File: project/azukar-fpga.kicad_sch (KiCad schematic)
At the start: 11 parts

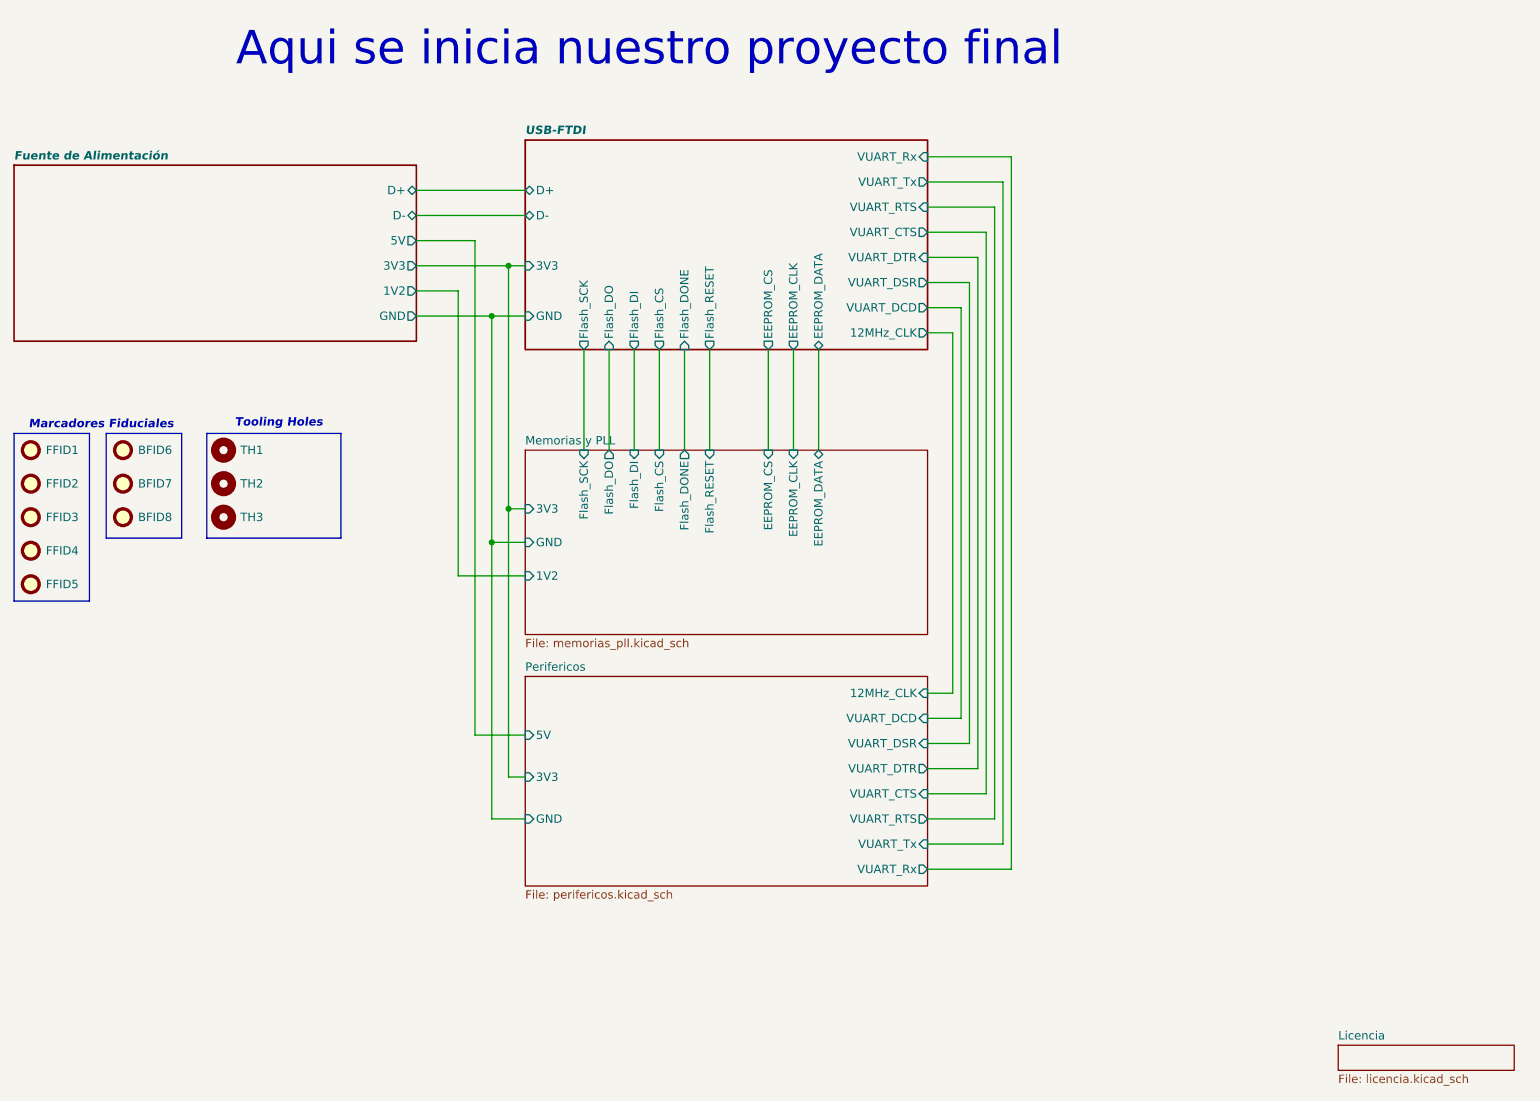
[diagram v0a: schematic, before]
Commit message: cambio a nombre final, agregado de licencia en esquematico y etiqueta
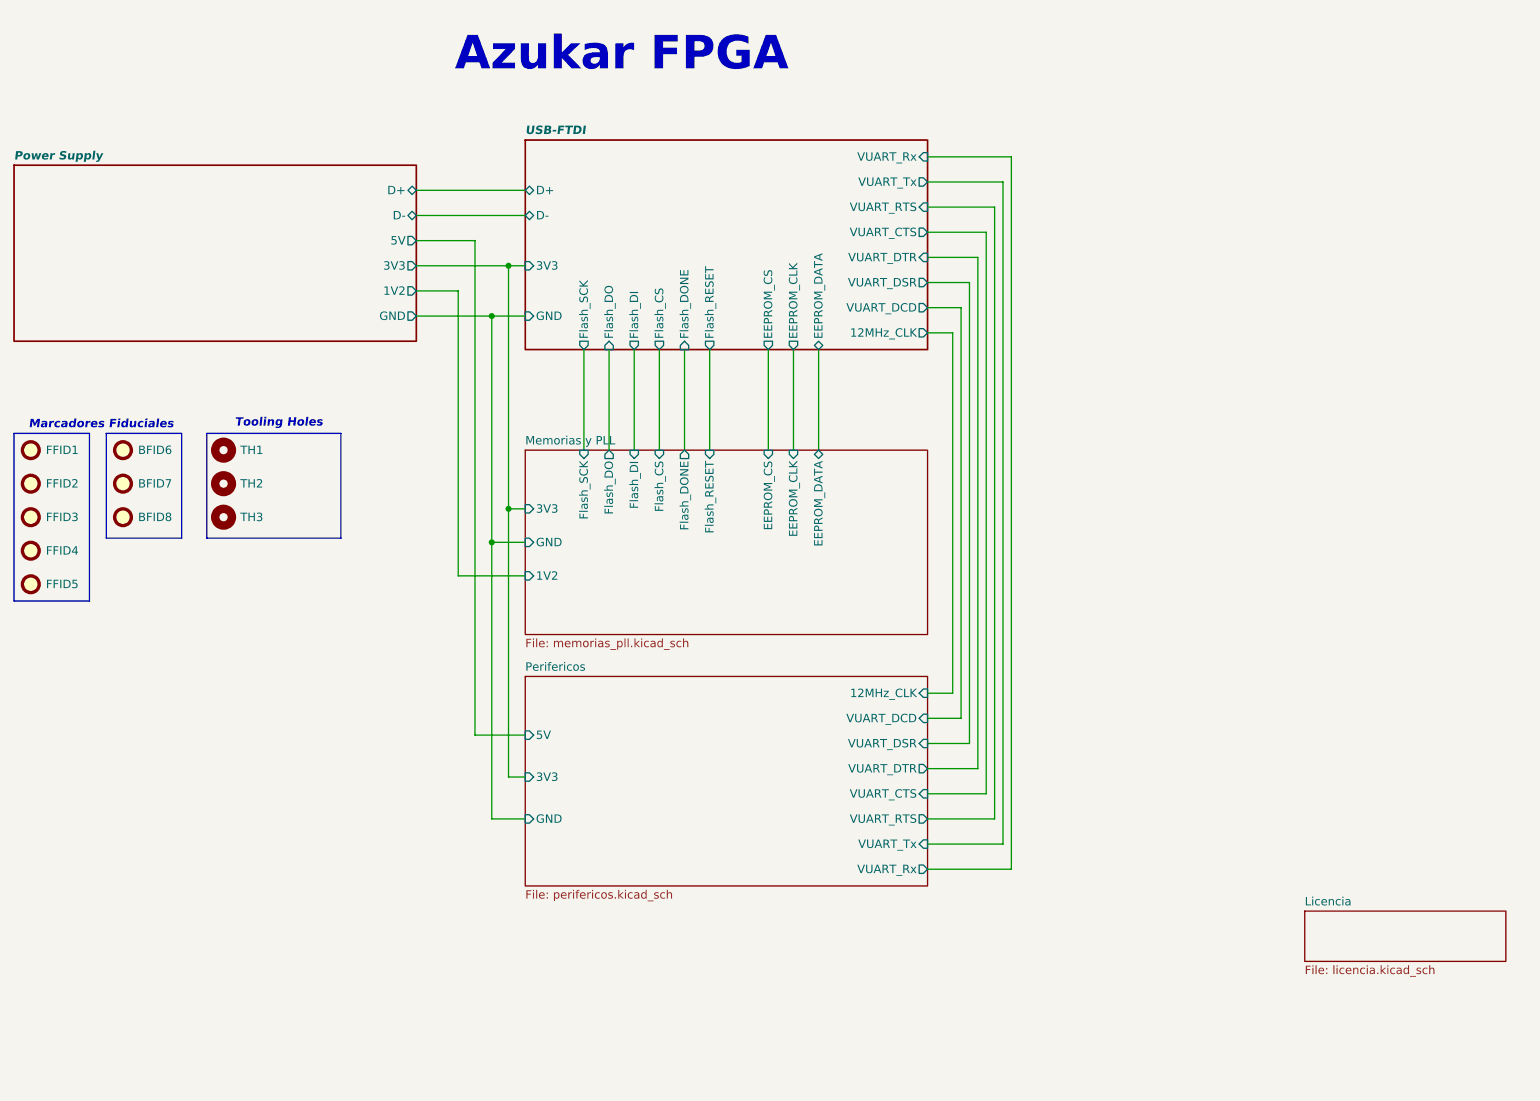
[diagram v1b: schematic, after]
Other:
- sheet Fuente de Alimentación renamed Power Supply
- note added: "Azukar FPGA"
- note removed: "Aqui se inicia nuestro proyecto final"
- company: (none) -> Maximiliano Simonazzi, Valentin Gomez Espeche
- title: (none) -> Azukar FPGA
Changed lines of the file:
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@@
 	(generator_version "9.0")
 	(paper "A4")
+	(title_block
+		(title "Azukar FPGA")
+		(date "2026-02-04")
+		(rev "1.4")
+		(company "Maximiliano Simonazzi, Valentin Gomez Espeche")
+		(comment 1 "attribution to the original AZUKAR project is preserved.")
+		(comment 2 "This design may be copied, modified, manufactured, and distributed provided that")
+		(comment 3 "Year: 2026")
+		(comment 4 "License: CERN Open Hardware Licence v2 – Permissive (CERN-OHL-P-2.0)")
+	)
 	(rectangle
 		(start 83.82 81.28)
@@
 		)
 	)
-	(text "Aqui se inicia nuestro proyecto final"
+	(text "Azukar FPGA"
 		(exclude_from_sim no)
-		(at 150.876 23.114 0)
+		(at 121.412 23.876 0)
 		(effects
 			(font
 				(size 5.08 5.08)
-			)
+				(thickness 1.016)
+				(bold yes)
+			)
+			(justify left)
 		)
 	)
@@
 		)
 		(instances
-			(project "fpga-utn"
+			(project "azukar-fpga"
 				(path "/fadb8841-cd7a-4174-937d-7c393e857c90"
 					(reference "FFID4")
@@
 		)
 		(instances
-			(project "fpga-utn"
+			(project "azukar-fpga"
 				(path "/fadb8841-cd7a-4174-937d-7c393e857c90"
 					(reference "FFID5")
@@
 		)
 		(instances
-			(project "fpga-utn"
+			(project "azukar-fpga"
 				(path "/fadb8841-cd7a-4174-937d-7c393e857c90"
 					(reference "BFID8")
@@
 		)
 		(instances
-			(project "fpga-utn"
+			(project "azukar-fpga"
 				(path "/fadb8841-cd7a-4174-937d-7c393e857c90"
 					(reference "FFID3")
@@
 		)
 		(instances
-			(project "fpga-utn"
+			(project "azukar-fpga"
 				(path "/fadb8841-cd7a-4174-937d-7c393e857c90"
 					(reference "BFID7")
@@
 		)
 		(instances
-			(project "fpga-utn"
+			(project "azukar-fpga"
 				(path "/fadb8841-cd7a-4174-937d-7c393e857c90"
 					(reference "FFID2")
@@
 		)
 		(instances
-			(project "fpga-utn"
+			(project "azukar-fpga"
 				(path "/fadb8841-cd7a-4174-937d-7c393e857c90"
 					(reference "BFID6")
@@
 		)
 		(instances
-			(project "fpga-utn"
+			(project "azukar-fpga"
 				(path "/fadb8841-cd7a-4174-937d-7c393e857c90"
 					(page "5")
@@
 	)
 	(sheet
-		(at 255.27 173.99)
-		(size 26.67 3.81)
+		(at 250.19 153.67)
+		(size 30.48 7.62)
 		(exclude_from_sim no)
 		(in_bom yes)
@@
 		)
 		(property "Sheetname" "Licencia"
-			(at 255.27 173.2784 0)
+			(at 250.19 152.9584 0)
 			(effects
 				(font
@@
 		)
 		(property "Sheetfile" "licencia.kicad_sch"
-			(at 255.27 178.3846 0)
+			(at 250.19 161.8746 0)
 			(effects
 				(font
@@
 		)
 		(instances
-			(project "fpga-utn"
+			(project "azukar-fpga"
 				(path "/fadb8841-cd7a-4174-937d-7c393e857c90"
 					(page "6")
@@
 		)
 		(instances
-			(project "fpga-utn"
+			(project "azukar-fpga"
 				(path "/fadb8841-cd7a-4174-937d-7c393e857c90"
 					(page "3")
@@
 			(color 0 0 0 0.0000)
 		)
-		(property "Sheetname" "Fuente de Alimentación"
+		(property "Sheetname" "Power Supply"
 			(at 54.61 39.9284 0)
 			(effects
@@
 		)
 		(instances
-			(project "fpga-utn"
+			(project "azukar-fpga"
 				(path "/fadb8841-cd7a-4174-937d-7c393e857c90"
 					(page "2")
@@
 		)
 		(instances
-			(project "fpga-utn"
+			(project "azukar-fpga"
 				(path "/fadb8841-cd7a-4174-937d-7c393e857c90"
 					(page "4")

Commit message: Eliminar mensaje de error - Issue #8. Mejora en algunas trazas del PCB, eliminacion de algunas vias ordenando mejor los componentes.
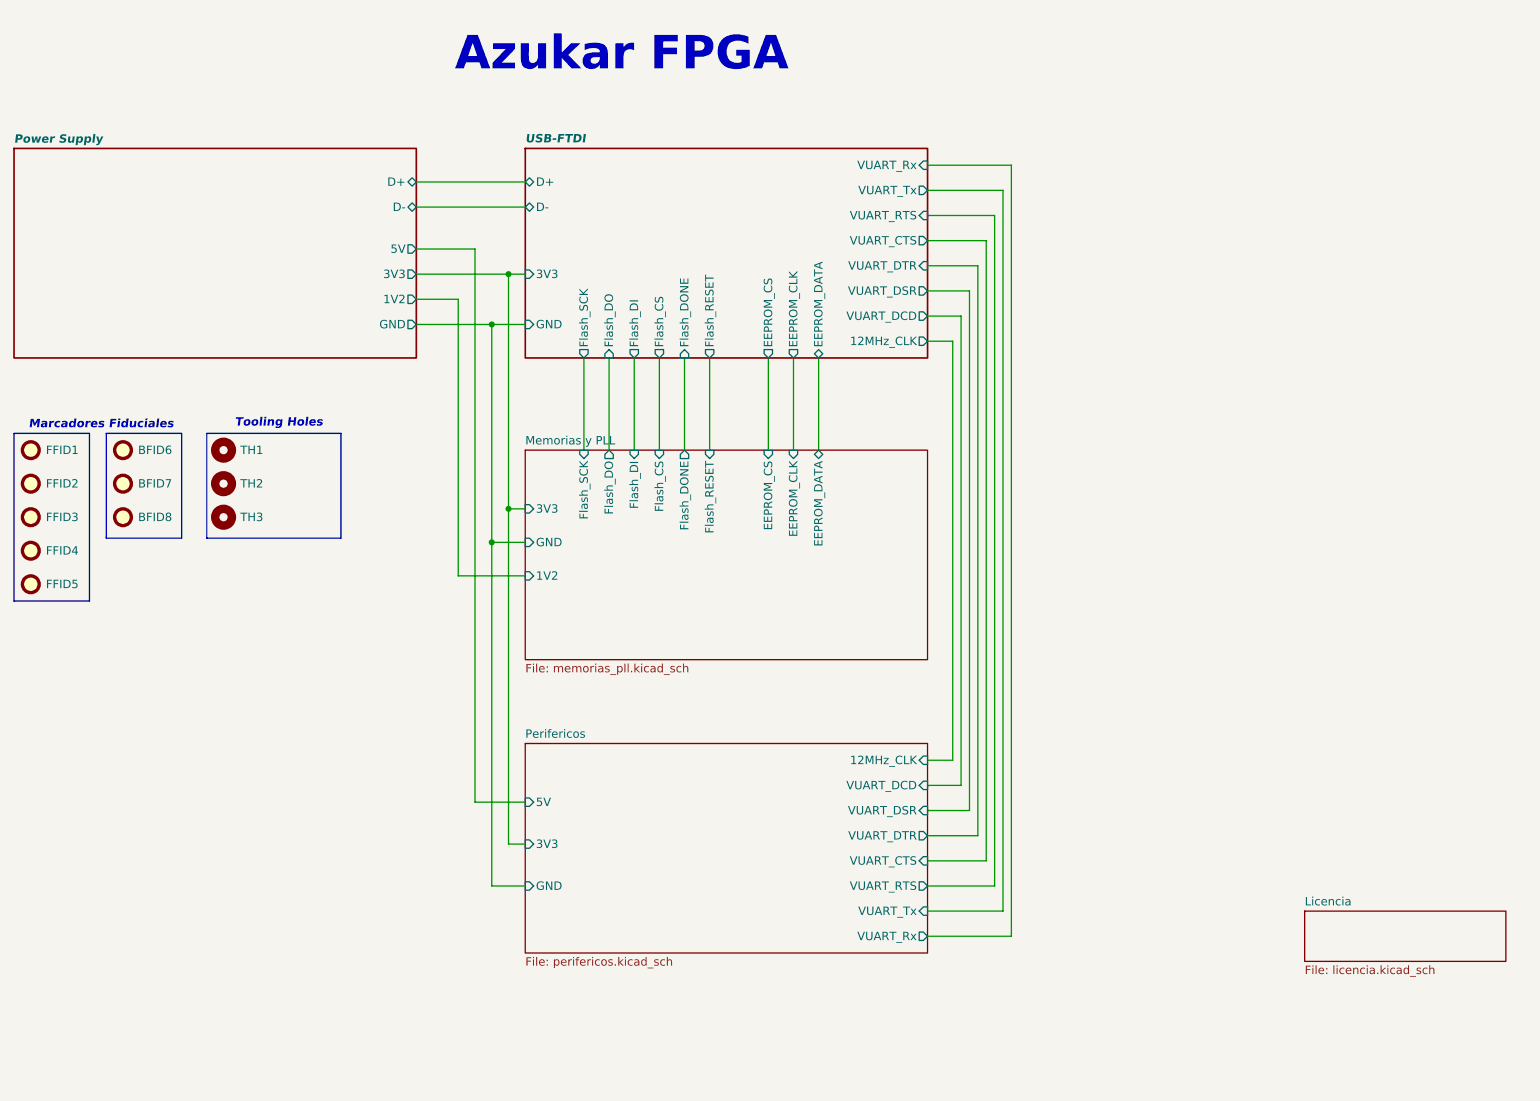
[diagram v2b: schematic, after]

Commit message: Version 2 de pcb completa, falta revisar silkscreen y ajustes menores
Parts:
- renumbered BFID6 to BFID1, BFID7 to BFID2, BFID8 to BFID3
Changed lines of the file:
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@@
 		(title "Azukar FPGA")
 		(date "2026-02-04")
-		(rev "1.4")
+		(rev "2.0")
 		(company "Maximiliano Simonazzi, Valentin Gomez Espeche")
 		(comment 1 "attribution to the original AZUKAR project is preserved.")
@@
 		(on_board yes)
 		(dnp no)
-		(property "Reference" "BFID8"
+		(property "Reference" "BFID3"
 			(at 73.406 93.98 0)
 			(effects
@@
 			(project "azukar-fpga"
 				(path "/fadb8841-cd7a-4174-937d-7c393e857c90"
-					(reference "BFID8")
+					(reference "BFID3")
 					(unit 1)
 				)
@@
 		(on_board yes)
 		(dnp no)
-		(property "Reference" "BFID7"
+		(property "Reference" "BFID2"
 			(at 73.406 88.9 0)
 			(effects
@@
 			(project "azukar-fpga"
 				(path "/fadb8841-cd7a-4174-937d-7c393e857c90"
-					(reference "BFID7")
+					(reference "BFID2")
 					(unit 1)
 				)
@@
 		(on_board yes)
 		(dnp no)
-		(property "Reference" "BFID6"
+		(property "Reference" "BFID1"
 			(at 73.406 83.82 0)
 			(effects
@@
 			(project "azukar-fpga"
 				(path "/fadb8841-cd7a-4174-937d-7c393e857c90"
-					(reference "BFID6")
+					(reference "BFID1")
 					(unit 1)
 				)

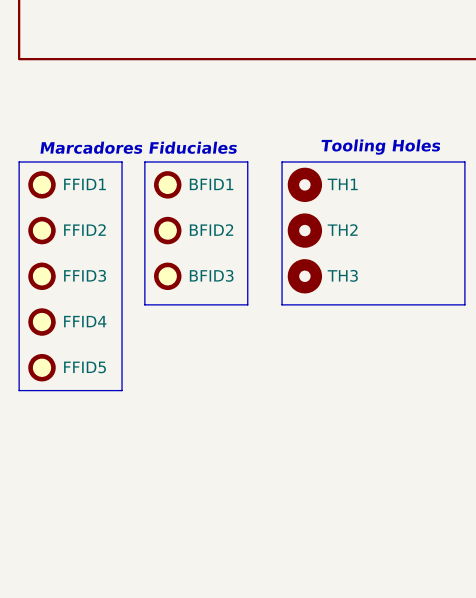
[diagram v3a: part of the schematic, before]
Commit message: Reordenadas las resistencias y capacitores de los botones y separaciones
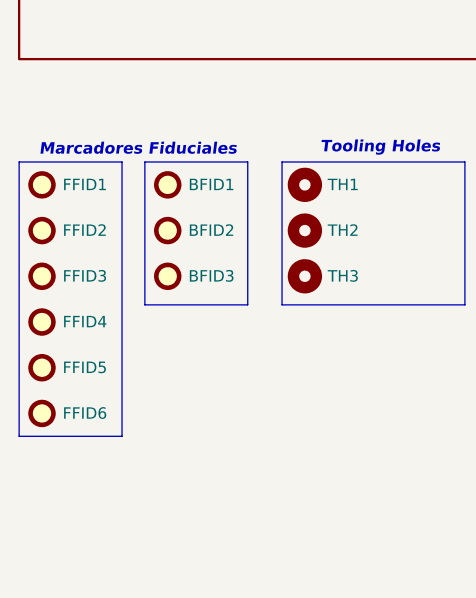
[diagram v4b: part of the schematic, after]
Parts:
- added FFID6: Fiducial, Fiducial:Fiducial_1mm_Mask2mm, symbol Mechanical:Fiducial
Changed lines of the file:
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@@
 	(rectangle
 		(start 54.61 81.28)
-		(end 66.04 106.68)
+		(end 66.04 111.76)
 		(stroke
 			(width 0)
@@
 					(unit 1)
 				)
+			)
+		)
+	)
+	(symbol
+		(lib_id "Mechanical:Fiducial")
+		(at 57.15 109.22 0)
+		(unit 1)
+		(exclude_from_sim no)
+		(in_bom yes)
+		(on_board yes)
+		(dnp no)
+		(property "Reference" "FFID6"
+			(at 59.436 109.22 0)
+			(effects
+				(font
+					(size 1.27 1.27)
+				)
+				(justify left)
+			)
+		)
+		(property "Value" "Fiducial"
+			(at 59.69 110.4899 0)
+			(effects
+				(font
+					(size 1.27 1.27)
+				)
+				(justify left)
+				(hide yes)
+			)
+		)
+		(property "Footprint" "Fiducial:Fiducial_1mm_Mask2mm"
+			(at 57.15 109.22 0)
+			(effects
+				(font
+					(size 1.27 1.27)
+				)
+				(hide yes)
+			)
+		)
+		(property "Datasheet" "~"
+			(at 57.15 109.22 0)
+			(effects
+				(font
+					(size 1.27 1.27)
+				)
+				(hide yes)
+			)
+		)
+		(property "Description" "Fiducial Marker"
+			(at 57.15 109.22 0)
+			(effects
+				(font
+					(size 1.27 1.27)
+				)
+				(hide yes)
+			)
+		)
+		(property "Hoja de datos del vendedor" ""
+			(at 57.15 109.22 0)
+			(effects
+				(font
+					(size 1.27 1.27)
+				)
+				(hide yes)
+			)
+		)
+		(property "Link del vendedor" ""
+			(at 57.15 109.22 0)
+			(effects
+				(font
+					(size 1.27 1.27)
+				)
+				(hide yes)
+			)
+		)
+		(property "Nombre de la hoja de datos" ""
+			(at 57.15 109.22 0)
+			(effects
+				(font
+					(size 1.27 1.27)
+				)
+				(hide yes)
+			)
+		)
+		(property "Tecnología" ""
+			(at 57.15 109.22 0)
+			(effects
+				(font
+					(size 1.27 1.27)
+				)
+				(hide yes)
+			)
+		)
+		(instances
+			(project "azukar-fpga"
+				(path "/fadb8841-cd7a-4174-937d-7c393e857c90"
+					(reference "FFID6")
+					(unit 1)
+				)
